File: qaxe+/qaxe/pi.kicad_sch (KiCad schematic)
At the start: 45 parts, among them J4 Conn_01x02, J5 Conn_01x02, J5 SWD, J6 USB_C_Receptacle_USB2.0, M2 Fan_4pin, SW1 boot, U13 TMP1075, U35 STM32L151CCT6, U37 TXU0101, U39 TXU0101, X1 8MHz

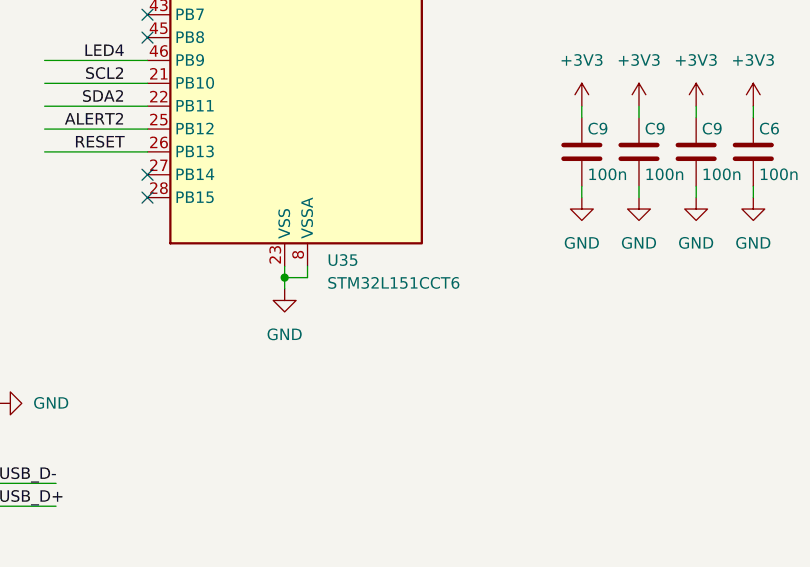
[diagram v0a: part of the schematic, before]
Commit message: updated qaxe+ to L072
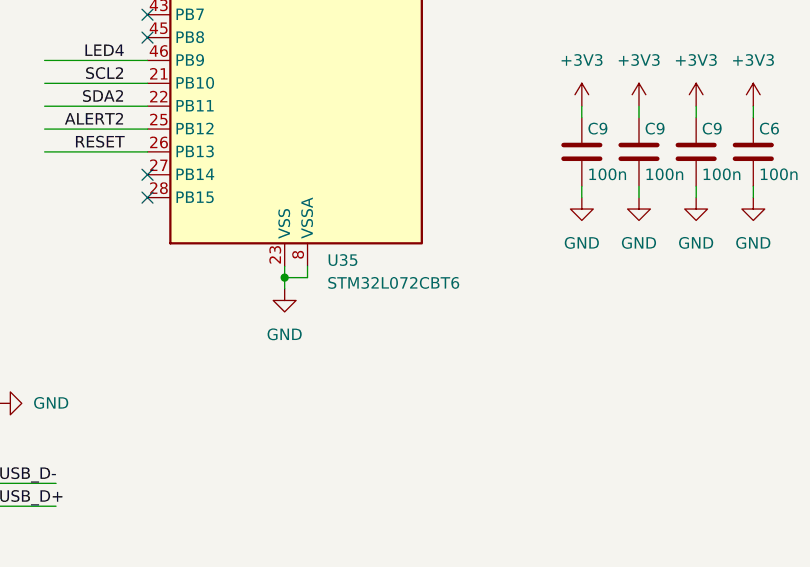
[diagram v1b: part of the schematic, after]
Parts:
- U35: value STM32L151CCT6 -> STM32L072CBT6; Manufacturer STM32L151CCT6 -> STM32L072CBT6; OrderNr 497-19371-1-ND -> 497-17503-ND
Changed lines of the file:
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@@
 			)
 		)
-		(property "Value" "STM32L151CCT6"
+		(property "Value" "STM32L072CBT6"
 			(at 96.1741 118.745 0)
 			(effects
@@
 			)
 		)
-		(property "Manufacturer" "STM32L151CCT6"
+		(property "Manufacturer" "STM32L072CBT6"
 			(at 91.44 78.74 0)
 			(effects
@@
 			)
 		)
-		(property "OrderNr" "497-19371-1-ND"
+		(property "OrderNr" "497-17503-ND"
 			(at 91.44 78.74 0)
 			(effects

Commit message: qaxe+
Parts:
- U35: value STM32L072CBT6 -> STM32L151CCT6; Manufacturer STM32L072CBT6 -> STM32L151CCT6; OrderNr 497-17503-ND -> 497-19371-1-ND
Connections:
- net LDO_EN: now reaches U35.17 (PA7)
- no-connect marks 22 -> 21
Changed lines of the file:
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@@
 	)
 	(no_connect
-		(at 109.22 60.96)
-	)
-	(no_connect
 		(at 76.2 78.74)
 	)
@@
 	(wire
 		(pts
+			(xy 109.22 60.96) (xy 120.65 60.96)
+		)
+		(stroke
+			(width 0)
+			(type default)
+		)
+	)
+	(wire
+		(pts
 			(xy 109.22 76.2) (xy 123.19 76.2)
 		)
@@
 		)
 	)
+	(global_label "LDO_EN"
+		(shape output)
+		(at 120.65 60.96 0)
+		(fields_autoplaced yes)
+		(effects
+			(font
+				(size 1.27 1.27)
+			)
+			(justify left)
+		)
+		(property "Intersheetrefs" "${INTERSHEET_REFS}"
+			(at 130.7109 60.96 0)
+			(effects
+				(font
+					(size 1.27 1.27)
+				)
+				(justify left)
+				(hide yes)
+			)
+		)
+	)
 	(hierarchical_label "RXD"
 		(shape input)
@@
 			)
 		)
-		(property "Value" "STM32L072CBT6"
+		(property "Value" "STM32L151CCT6"
 			(at 96.1741 118.745 0)
 			(effects
@@
 			)
 		)
-		(property "Manufacturer" "STM32L072CBT6"
+		(property "Manufacturer" "STM32L151CCT6"
 			(at 91.44 78.74 0)
 			(effects
@@
 			)
 		)
-		(property "OrderNr" "497-17503-ND"
+		(property "OrderNr" "497-19371-1-ND"
 			(at 91.44 78.74 0)
 			(effects

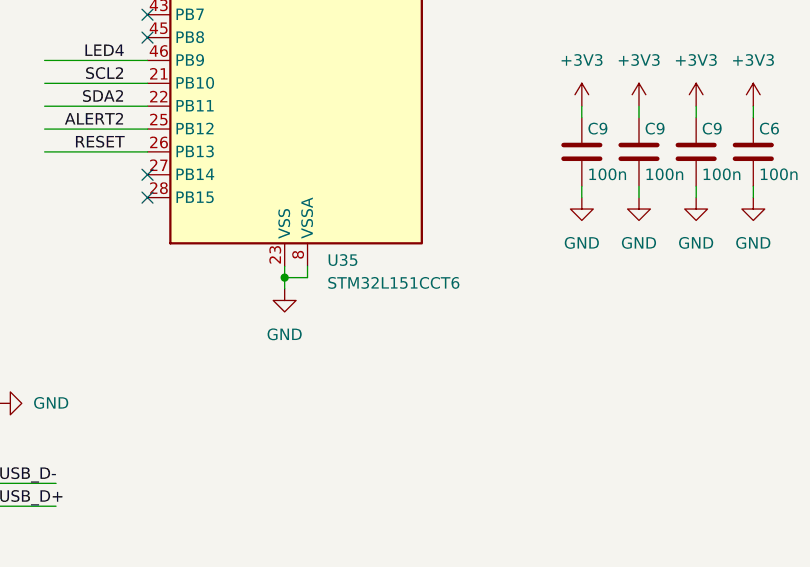
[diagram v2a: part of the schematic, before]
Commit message: updated L151 with L072 for qaxe+
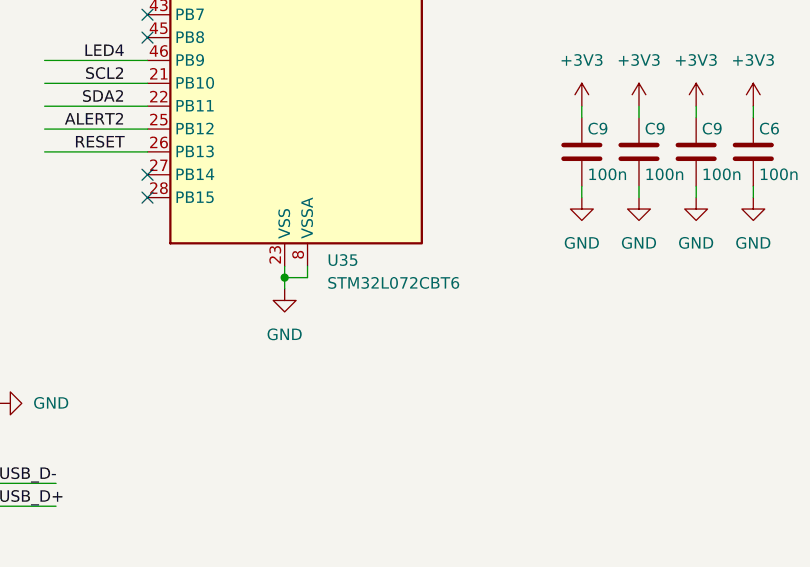
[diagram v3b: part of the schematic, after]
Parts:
- U35: value STM32L151CCT6 -> STM32L072CBT6; Manufacturer STM32L151CCT6 -> STM32L072CBT6; OrderNr 497-19371-1-ND -> 497-17503-ND
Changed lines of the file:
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@@
 			)
 		)
-		(property "Value" "STM32L151CCT6"
+		(property "Value" "STM32L072CBT6"
 			(at 96.1741 118.745 0)
 			(effects
@@
 			)
 		)
-		(property "Manufacturer" "STM32L151CCT6"
+		(property "Manufacturer" "STM32L072CBT6"
 			(at 91.44 78.74 0)
 			(effects
@@
 			)
 		)
-		(property "OrderNr" "497-19371-1-ND"
+		(property "OrderNr" "497-17503-ND"
 			(at 91.44 78.74 0)
 			(effects

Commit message: some bom fixes
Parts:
- J4, J5, R30, R31: now not fitted; now left out of the parts list
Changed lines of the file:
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@@
 		(unit 1)
 		(exclude_from_sim no)
-		(in_bom yes)
+		(in_bom no)
 		(on_board yes)
-		(dnp no)
+		(dnp yes)
 		(fields_autoplaced yes)
 		(property "Reference" "J5"
@@
 		(unit 1)
 		(exclude_from_sim no)
-		(in_bom yes)
+		(in_bom no)
 		(on_board yes)
-		(dnp no)
+		(dnp yes)
 		(property "Reference" "R30"
 			(at 135.89 166.37 0)
@@
 		(unit 1)
 		(exclude_from_sim no)
-		(in_bom yes)
+		(in_bom no)
 		(on_board yes)
-		(dnp no)
+		(dnp yes)
 		(property "Reference" "R31"
 			(at 148.59 166.37 0)
@@
 		(unit 1)
 		(exclude_from_sim no)
-		(in_bom yes)
+		(in_bom no)
 		(on_board yes)
-		(dnp no)
+		(dnp yes)
 		(fields_autoplaced yes)
 		(property "Reference" "J4"
